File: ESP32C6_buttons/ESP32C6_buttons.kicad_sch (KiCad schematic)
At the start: 6 parts, among them J1 Power, SW1 SW_Push, SW2 SW_Push, SW3 SW_Push, SW4 SW_Push, U1 XIAO-ESP32-C6-DIP

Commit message: add buttons
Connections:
- net +3V3: now also J1.2 (Pin_2); no longer J1.1 (Pin_1)
- net GND: now also J1.1 (Pin_1); no longer J1.2 (Pin_2)
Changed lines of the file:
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@@
 	(symbol
 		(lib_id "Connector:Conn_01x02_Socket")
-		(at 184.15 111.76 0)
+		(at 184.15 114.3 0)
+		(mirror x)
 		(unit 1)
 		(exclude_from_sim no)
@@
 		(on_board yes)
 		(dnp no)
-		(fields_autoplaced yes)
 		(property "Reference" "J1"
-			(at 185.42 111.7599 0)
+			(at 185.42 114.3001 0)
 			(effects
 				(font
@@
 		)
 		(property "Value" "Power"
-			(at 185.42 114.2999 0)
+			(at 185.42 111.7601 0)
 			(effects
 				(font
@@
 		)
 		(property "Footprint" "Connector_JST:JST_XH_B2B-XH-A_1x02_P2.50mm_Vertical"
-			(at 184.15 111.76 0)
+			(at 184.15 114.3 0)
 			(effects
 				(font
@@
 		)
 		(property "Datasheet" "~"
-			(at 184.15 111.76 0)
+			(at 184.15 114.3 0)
 			(effects
 				(font
@@
 		)
 		(property "Description" "Generic connector, single row, 01x02, script generated"
-			(at 184.15 111.76 0)
+			(at 184.15 114.3 0)
 			(effects
 				(font

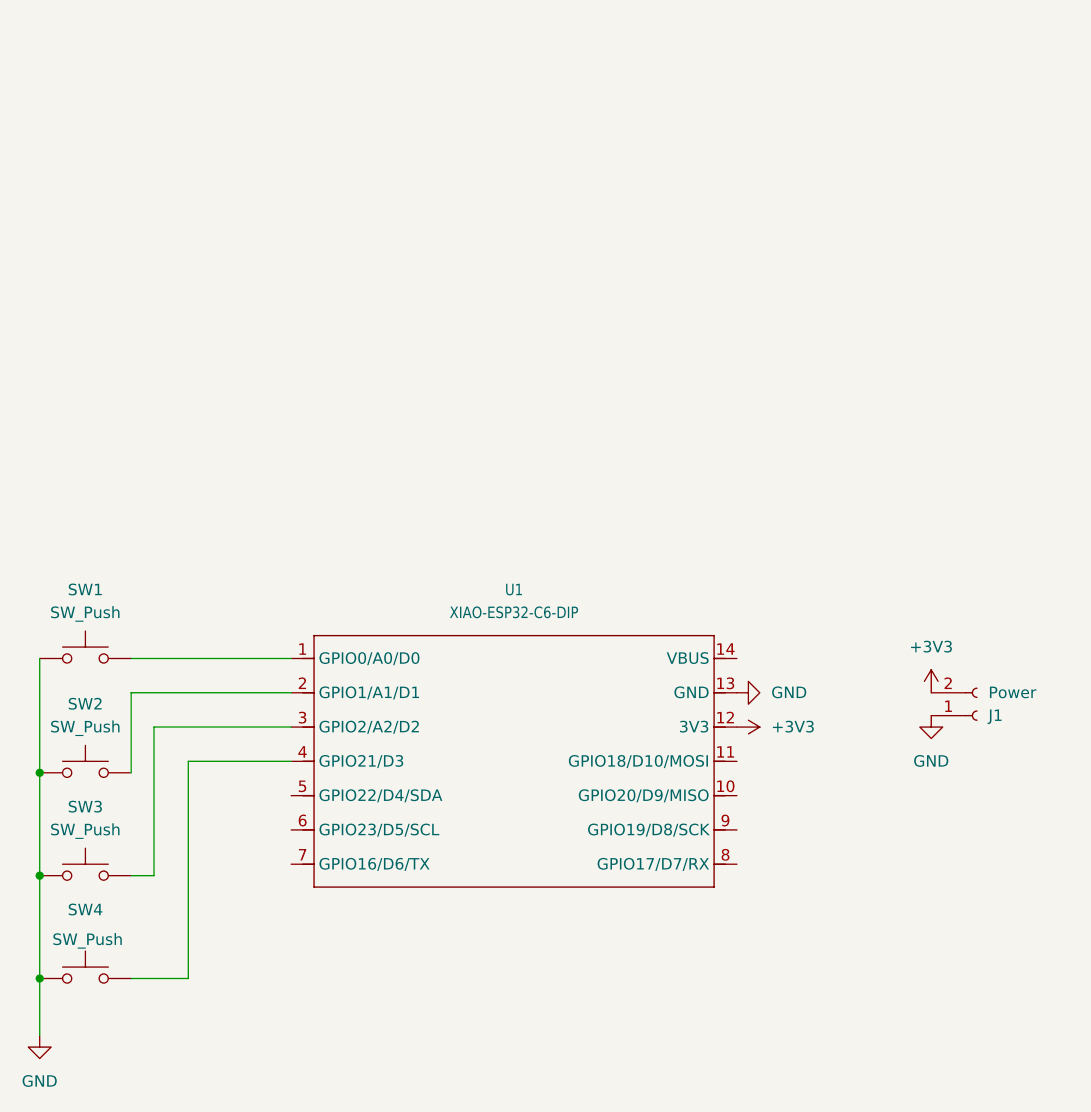
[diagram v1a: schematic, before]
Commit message: update to add rectifier
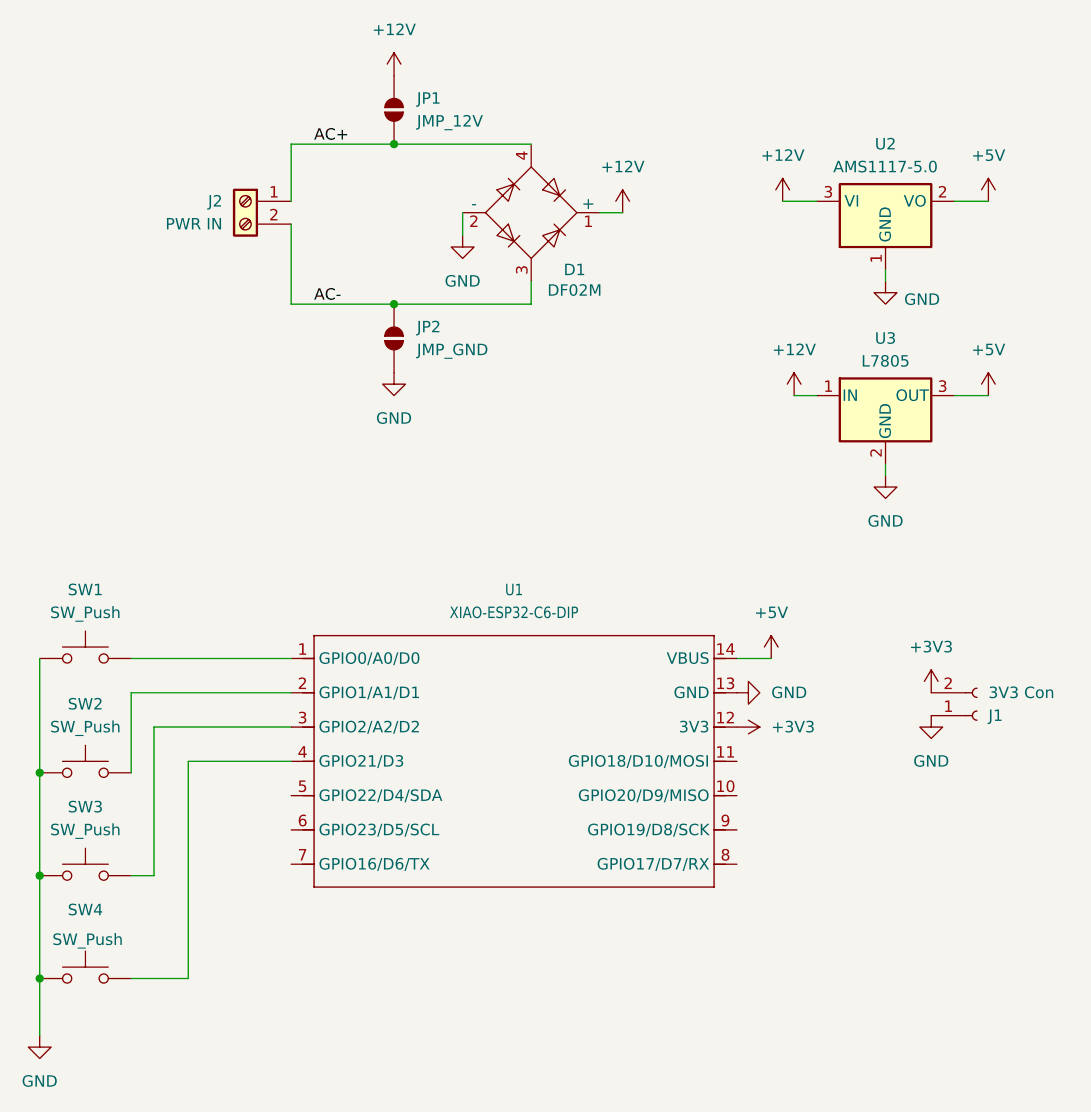
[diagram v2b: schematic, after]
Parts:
- added D1: DF02M, Diode_THT:Diode_Bridge_DIP-4_W7.62mm_P5.08mm, symbol Diode_Bridge:DF02M
- added J2: PWR IN, Connector_Phoenix_MC_HighVoltage:PhoenixContact_MCV_1,5_2-G-5.08_1x02_P5.08mm_Vertical, symbol Connector:Screw_Terminal_01x02
- added JP1: JMP_12V, Jumper:SolderJumper-2_P1.3mm_Open_Pad1.0x1.5mm, symbol Jumper:SolderJumper_2_Open
- added JP2: JMP_GND, Jumper:SolderJumper-2_P1.3mm_Open_Pad1.0x1.5mm, symbol Jumper:SolderJumper_2_Open
- added U2: AMS1117-5.0, Package_TO_SOT_SMD:SOT-223-3_TabPin2, symbol Regulator_Linear:AMS1117-5.0
- added U3: L7805, V_REG:OKI-78SR_Horz, symbol Regulator_Linear:L7805
- J1: value Power -> 3V3 Con
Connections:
- net GND: now also D1.2 (-), JP2.1 (A), U2.1 (GND), U3.2 (GND)
- net +5V: now reaches U1.14 (VBUS)
- net +5V: now also U2.2 (VO), U3.3 (OUT)
- new net +12V: D1.1 (+), JP1.2 (B), U2.3 (VI), U3.1 (IN)
- new net AC+: D1.4, J2.1 (Pin_1), JP1.1 (A)
- new net AC-: D1.3, J2.2 (Pin_2), JP2.2 (B)
